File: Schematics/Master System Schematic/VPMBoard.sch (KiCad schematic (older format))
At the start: 23 parts, among them J1 Charge_Signal, J14 Main_Signal, J15 Therm_Signal, J16 PumpIO, J17 GLV/Charge_PWR, J18 GND_QC, J19 BMS_Signal, J20 ThermEX_PWR, J21 BMS_PWR, Q1 FDP3632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

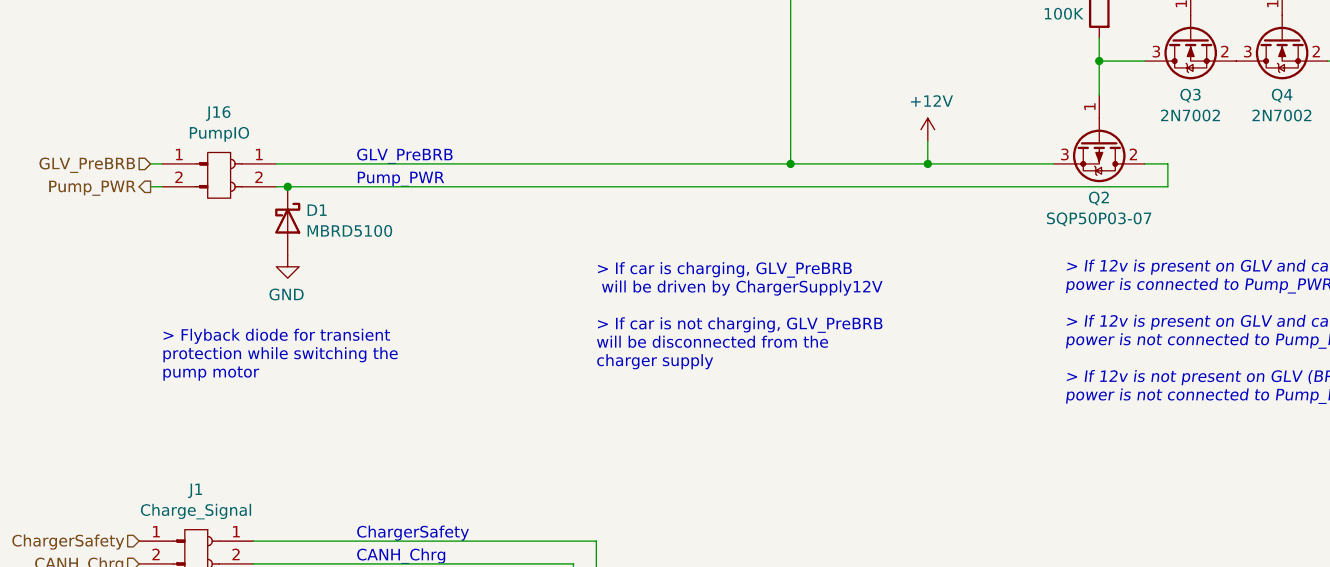
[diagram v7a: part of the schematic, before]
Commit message: Revert "VPM Board Flyback Diode"
This reverts commit 479d55be7c023c6502d2d4db07d9957a4b0a3a94.
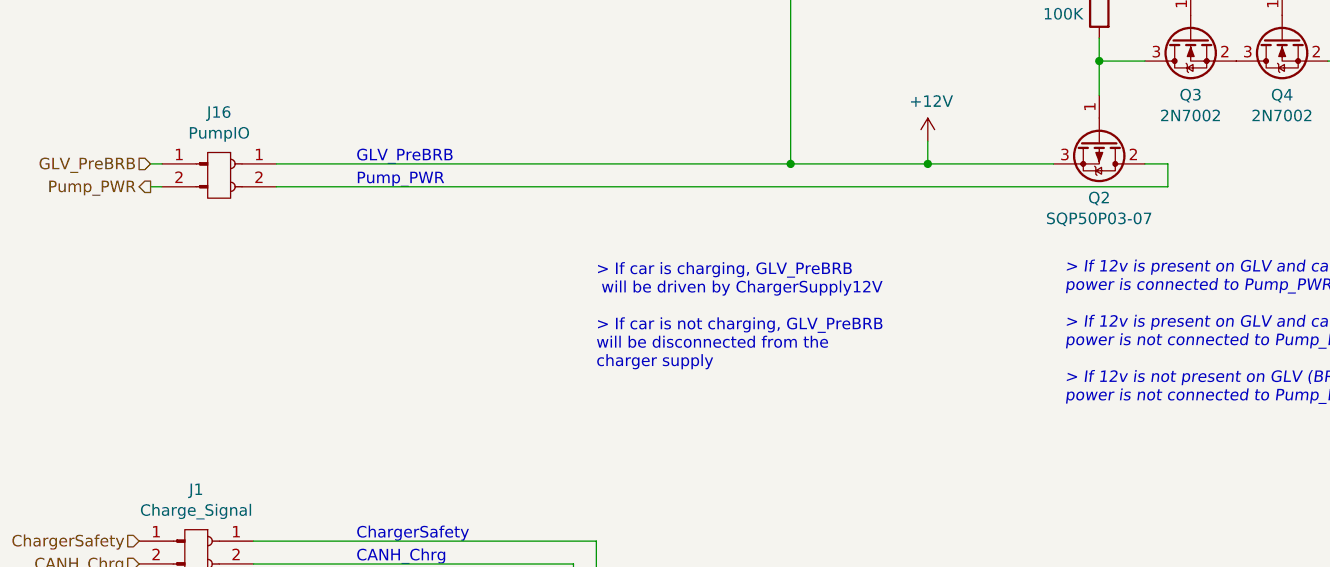
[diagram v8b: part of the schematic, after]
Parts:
- removed D1: MBRD5100, Diode_SMD:D_SOD-123, symbol Diode:MBR0520
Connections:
- new net: J1.1, J19.2
- new net: J1.2, J14.2, J15.2, J19.4
- new net: J1.3, J14.3, J15.3, J19.5
- new net: J14.1, J19.3
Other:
- note removed: "> Flyback diode for transient\nprotection while switching the \npump motor"
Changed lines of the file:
@@
 Sheet 22 23
 Title "Vehicle Power Management Board"
-Date "2021-02-11"
-Rev "4.3"
+Date "2021-01-30"
+Rev "4.2"
 Comp "Northeastern Electric Racing"
 Comment1 "https://github.com/Northeastern-Electric-Racing/NER"
@@
 	1750 3550 4000 3550
 Wire Wire Line
-	1750 3650 1800 3650
+	1750 3650 5650 3650
 Wire Wire Line
 	1250 3550 1200 3550
@@
 Wire Wire Line
 	4600 3550 5150 3550
-$Comp
-L Diode:MBR0520 D1
-U 1 1 602AC2AA
-P 1800 3800
-F 0 "D1" V 1754 3880 50  0000 L CNN
-F 1 "MBRD5100" V 1845 3880 50  0000 L CNN
-F 2 "Diode_SMD:D_SOD-123" H 1800 3625 50  0001 C CNN
-F 3 "http://www.mccsemi.com/up_pdf/MBR0520~MBR0580(SOD123).pdf" H 1800 3800 50  0001 C CNN
-	1    1800 3800
-	0    1    1    0
-$EndComp
-$Comp
-L power:GND #PWR014
-U 1 1 602ADBC9
-P 1800 3950
-F 0 "#PWR014" H 1800 3700 50  0001 C CNN
-F 1 "GND" H 1805 3777 50  0000 C CNN
-F 2 "" H 1800 3950 50  0001 C CNN
-F 3 "" H 1800 3950 50  0001 C CNN
-	1    1800 3950
-	-1   0    0    -1
-$EndComp
-Text Notes 1250 4500 0    50   ~ 0
-> Flyback diode for transient\nprotection while switching the \npump motor
-Connection ~ 1800 3650
-Wire Wire Line
-	1800 3650 5650 3650
 $EndSCHEMATC
